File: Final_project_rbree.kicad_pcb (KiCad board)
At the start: 2 copper layers, 96.3 x 77.7 mm, 49 parts, among them J1 Conn_01x02_Pin, J2 Conn_01x02_Pin, Q1 MMBT3904, Q2 AO3401A, U1 TL431DBZ, U2 LTV-817, U3 B1212, U4 2N7002, U7 NE555

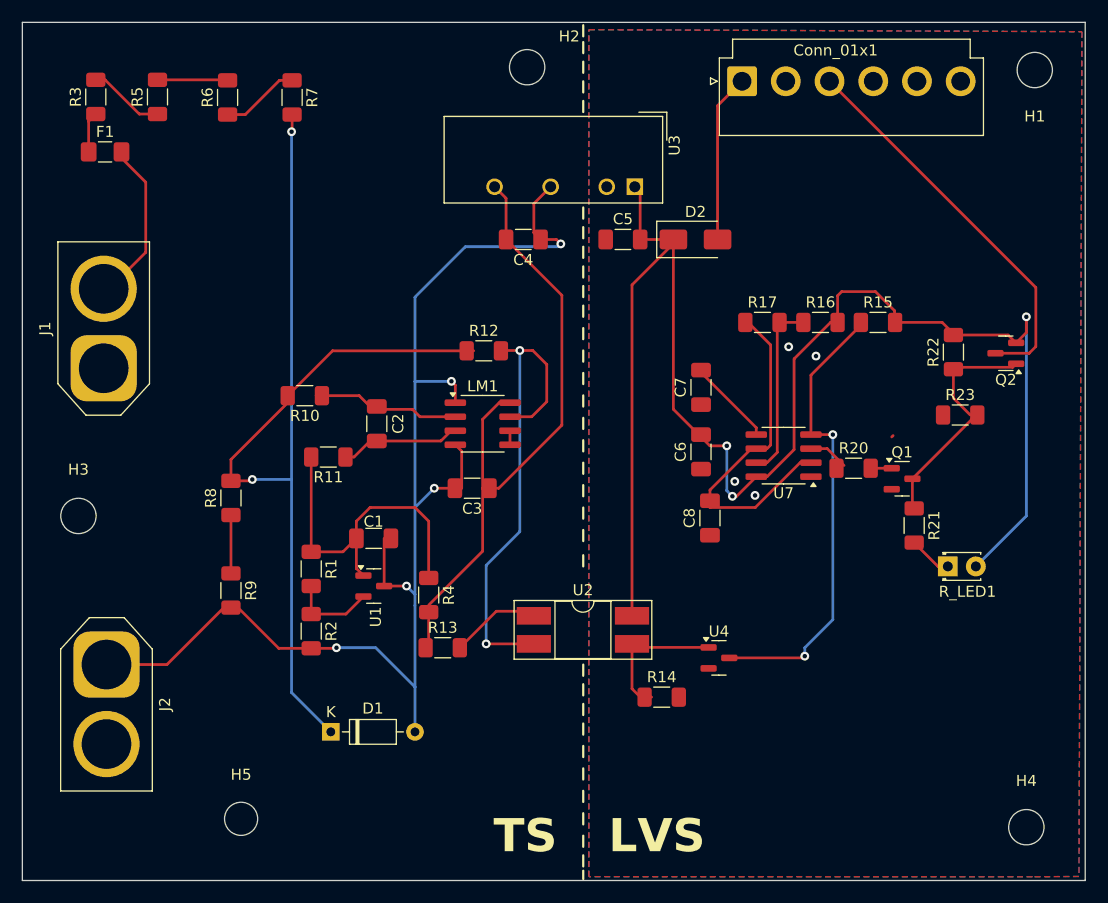
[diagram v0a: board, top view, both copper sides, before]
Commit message: added mounting holes positioning dimension, spacing of R15 R16R17 fixed
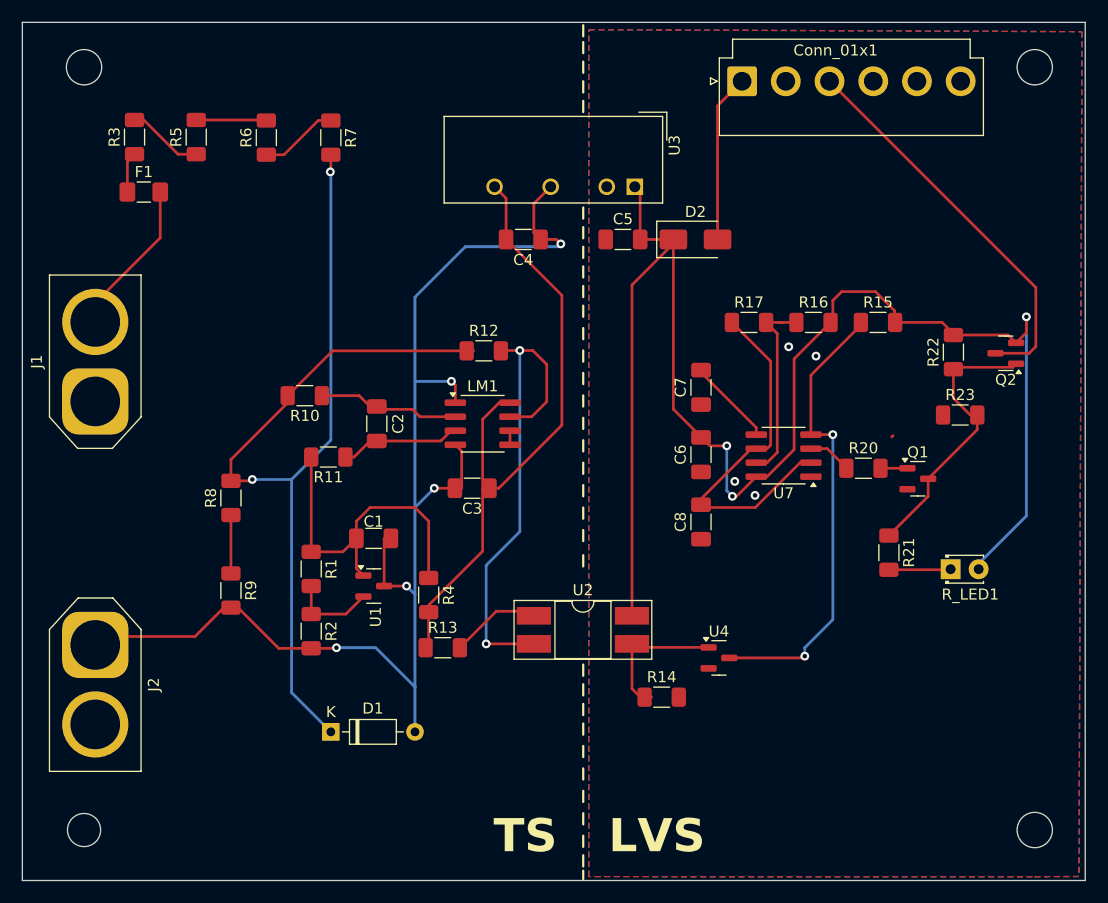
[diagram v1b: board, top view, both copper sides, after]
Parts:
- removed H3: MountingHole, MountingHole:MountingHole_3.2mm_M3
- moved H2 40.1 mm to (88.6, 70.1)
- moved H5 14.3 mm to (88.6, 139.2)
- moved R3 5.05 mm to (93.2, 76.4)
- moved R5 5.05 mm to (98.8, 76.4)
- moved R6 5.05 mm to (105.2, 76.5)
- moved R7 5.05 mm to (111.0, 76.5)
- moved F1 5.05 mm to (94.1, 81.4)
- moved R21 3.36 mm to (161.5, 114.1)
- moved J1 3.10 mm to (89.7, 100.4)
- moved J2 2.05 mm to (89.7, 122.4)
- moved Q1 1.43 mm to (164.2, 107.4)
- moved R17 1.22 mm to (148.9, 93.2)
- moved R20 0.89 mm to (159.2, 106.4)
- moved C8 0.88 mm to (144.5, 111.3)
- moved H4 0.80 mm to (174.8, 139.2)
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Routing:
- net Net-(J1-Pin_2): track 15.4 -> 11.4 mm
- net Net-(Q1-C): track 22.2 -> 25.0 mm
- net /Vin: track 91.3 -> 89.2 mm
- net Net-(U7-THR): track 31.5 -> 33.3 mm
- net Net-(R_LED1-K): track 3.94 -> 5.33 mm
- net Net-(U7-DIS): track 16.4 -> 17.5 mm
- net GND: track 117.3 -> 116.2 mm

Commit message: fixed messy TS
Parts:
- moved R12 16.2 mm to (108.7, 96.3)
- moved F1 4.49 mm to (89.9, 83.1)
- moved R3 4.36 mm to (89.9, 79.2), turned to 0 degrees
- moved R6 4.14 mm to (102.1, 79.2), turned to 180 degrees
- moved R5 3.98 mm to (96.0, 79.2), turned to 0 degrees
- moved R7 3.95 mm to (108.2, 79.2), turned to 0 degrees
- moved C2 2.49 mm to (117.6, 102.9)
- moved R11 2.17 mm to (108.7, 104.6)
- moved R4 1.33 mm to (121.2, 117.9), turned to 0 degrees
- moved R10 0.74 mm to (108.7, 100.6)
- moved D2 0.73 mm to (144.7, 85.6)
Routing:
- net Net-(LM1-Pad7): track 44.2 -> 59.5 mm
- net /Vin: track 89.2 -> 74.3 mm
- net Net-(R6-Pad1): track 7.13 -> 3.00 mm
- net Net-(R3-Pad2): track 6.74 -> 3.00 mm
- net /Vref: track 31.2 -> 34.6 mm
- net Net-(R5-Pad2): track 5.67 -> 3.00 mm
- net Net-(LM1--): track 10.9 -> 12.7 mm
- net Net-(LM1-+): track 13.4 -> 12.6 mm
- net Net-(J1-Pin_2): track 11.4 -> 10.8 mm

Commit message: minor ifx
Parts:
- H5: footprint MountingHole:MountingHole_3mm -> MountingHole:MountingHole_3.2mm_M3
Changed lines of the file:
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@@
 		(tags "resistor handsolder")
 		(property "Reference" "R5"
-			(at 0 -1.82 360)
+			(at 0 -1.82 0)
 			(layer "F.SilkS")
 			(effects
@@
 		)
 		(property "Value" "249k"
-			(at 0 1.82 360)
+			(at 0 1.82 0)
 			(layer "F.Fab")
 			(effects
@@
 		)
 		(fp_text user "${REFERENCE}"
-			(at 0 0 360)
+			(at 0 0 0)
 			(layer "F.Fab")
 			(effects
@@
 		(tags "resistor handsolder")
 		(property "Reference" "R4"
-			(at 0 -1.82 360)
+			(at 0 -1.82 0)
 			(layer "F.SilkS")
 			(effects
@@
 		)
 		(property "Value" "2k2"
-			(at 0 1.82 360)
+			(at 0 1.82 0)
 			(layer "F.Fab")
 			(effects
@@
 		)
 		(fp_text user "${REFERENCE}"
-			(at 0 0 360)
+			(at 0 0 0)
 			(layer "F.Fab")
 			(effects
@@
 		)
 	)
-	(footprint "MountingHole:MountingHole_3mm"
+	(footprint "MountingHole:MountingHole_3.2mm_M3"
 		(layer "F.Cu")
 		(at 88.646 139.192)
-		(descr "Mounting Hole 3mm, no annular")
-		(tags "mounting hole 3mm no annular")
+		(descr "Mounting Hole 3.2mm, no annular, M3")
+		(tags "mounting hole 3.2mm no annular m3")
 		(property "Reference" "H5"
-			(at 0 -4 0)
+			(at 0 -4.2 0)
 			(layer "F.SilkS")
-			(hide yes)
 			(effects
 				(font
@@
 		)
 		(property "Value" "MountingHole"
-			(at 0 -5.842 0)
+			(at 0 4.2 0)
 			(layer "F.Fab")
 			(effects
@@
 			)
 		)
-		(property "Footprint" "MountingHole:MountingHole_3mm"
+		(property "Footprint" "MountingHole:MountingHole_3.2mm_M3"
 			(at 0 0 0)
 			(unlocked yes)
@@
 		(fp_circle
 			(center 0 0)
-			(end 3 0)
+			(end 3.2 0)
 			(stroke
 				(width 0.15)
@@
 		(fp_circle
 			(center 0 0)
-			(end 3.25 0)
+			(end 3.45 0)
 			(stroke
 				(width 0.05)
@@
 		(pad "" np_thru_hole circle
 			(at 0 0)
-			(size 3 3)
-			(drill 3)
+			(size 3.2 3.2)
+			(drill 3.2)
 			(layers "*.Cu" "*.Mask")
 		)
@@
 		(tags "resistor handsolder")
 		(property "Reference" "R6"
-			(at -0.026001 1.778 360)
+			(at -0.026001 1.778 0)
 			(layer "F.SilkS")
 			(effects
@@
 		)
 		(property "Value" "249k"
-			(at -0.026001 -1.778 360)
+			(at -0.026001 -1.778 0)
 			(layer "F.Fab")
 			(effects
@@
 		)
 		(fp_text user "${REFERENCE}"
-			(at 0 0 360)
+			(at 0 0 0)
 			(layer "F.Fab")
 			(effects
@@
 		(tags "resistor handsolder")
 		(property "Reference" "R3"
-			(at 0 -1.82 360)
+			(at 0 -1.82 0)
 			(layer "F.SilkS")
 			(effects
@@
 		)
 		(property "Value" "249k"
-			(at 0 1.82 360)
+			(at 0 1.82 0)
 			(layer "F.Fab")
 			(effects
@@
 		)
 		(fp_text user "${REFERENCE}"
-			(at 0 0 360)
+			(at 0 0 0)
 			(layer "F.Fab")
 			(effects
@@
 		(tags "resistor handsolder")
 		(property "Reference" "R7"
-			(at 0 -1.82 360)
+			(at 0 -1.82 0)
 			(layer "F.SilkS")
 			(effects
@@
 		)
 		(property "Value" "249k"
-			(at 0 1.82 360)
+			(at 0 1.82 0)
 			(layer "F.Fab")
 			(effects
@@
 		)
 		(fp_text user "${REFERENCE}"
-			(at 0 0 360)
+			(at 0 0 0)
 			(layer "F.Fab")
 			(effects
